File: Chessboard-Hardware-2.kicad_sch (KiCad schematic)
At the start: 1 part, among them J1 Raspberry_Pi_0

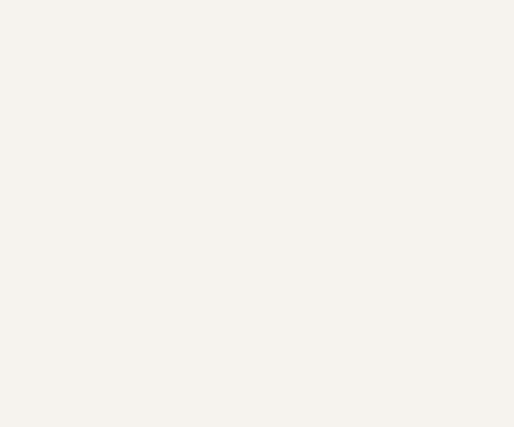
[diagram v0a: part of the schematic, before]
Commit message: Setup for chessboard layout
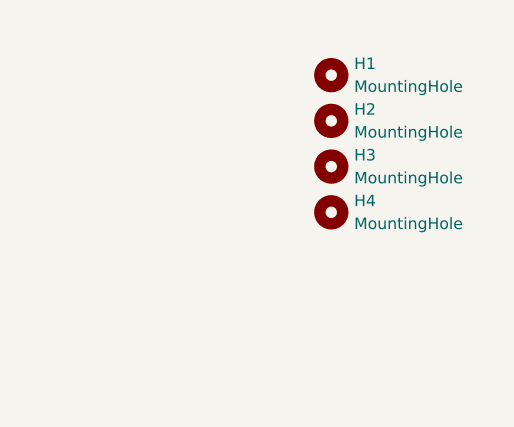
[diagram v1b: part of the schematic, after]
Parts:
- added H1, H2, H3, H4: MountingHole, MountingHole:MountingHole_2.7mm_M2.5, symbol Mechanical:MountingHole

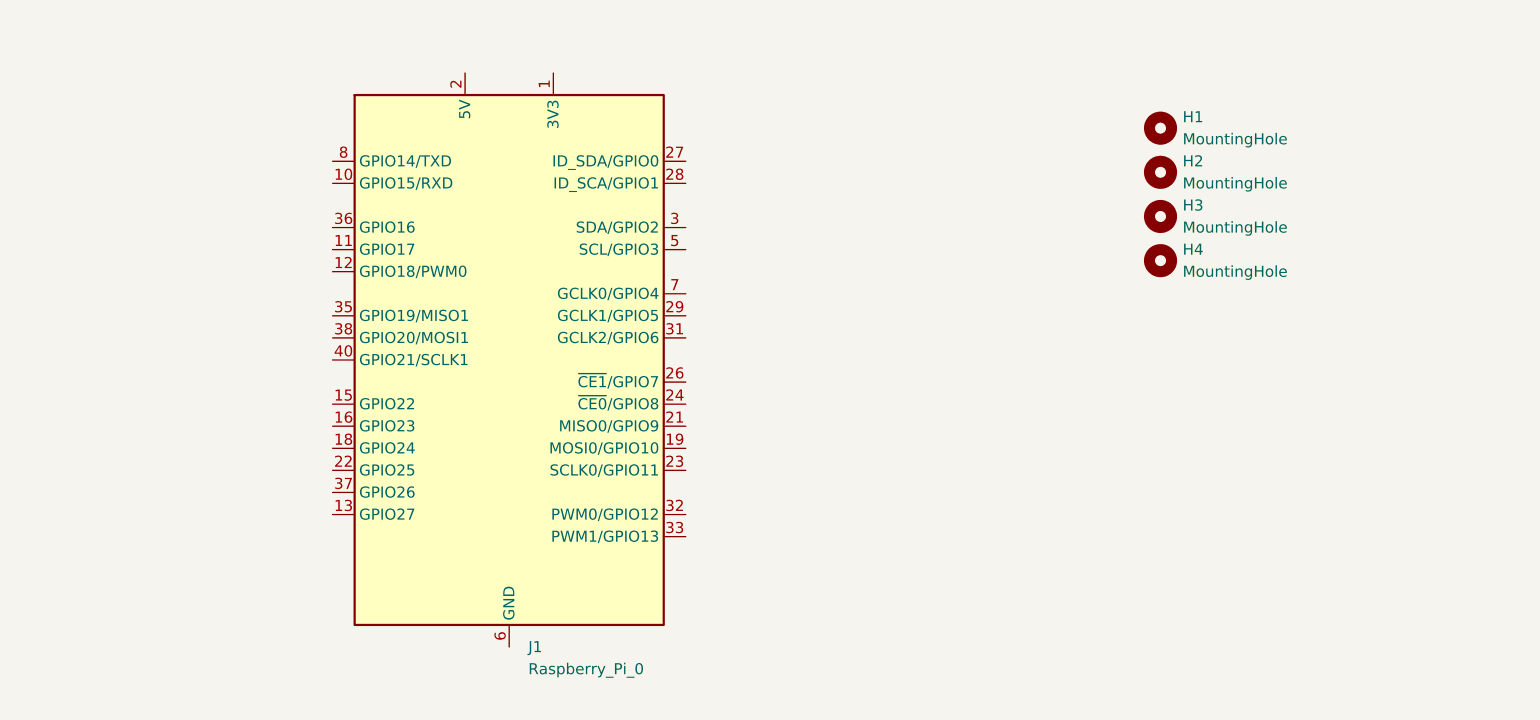
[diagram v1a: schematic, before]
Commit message: Add JST-XH connector and schematic
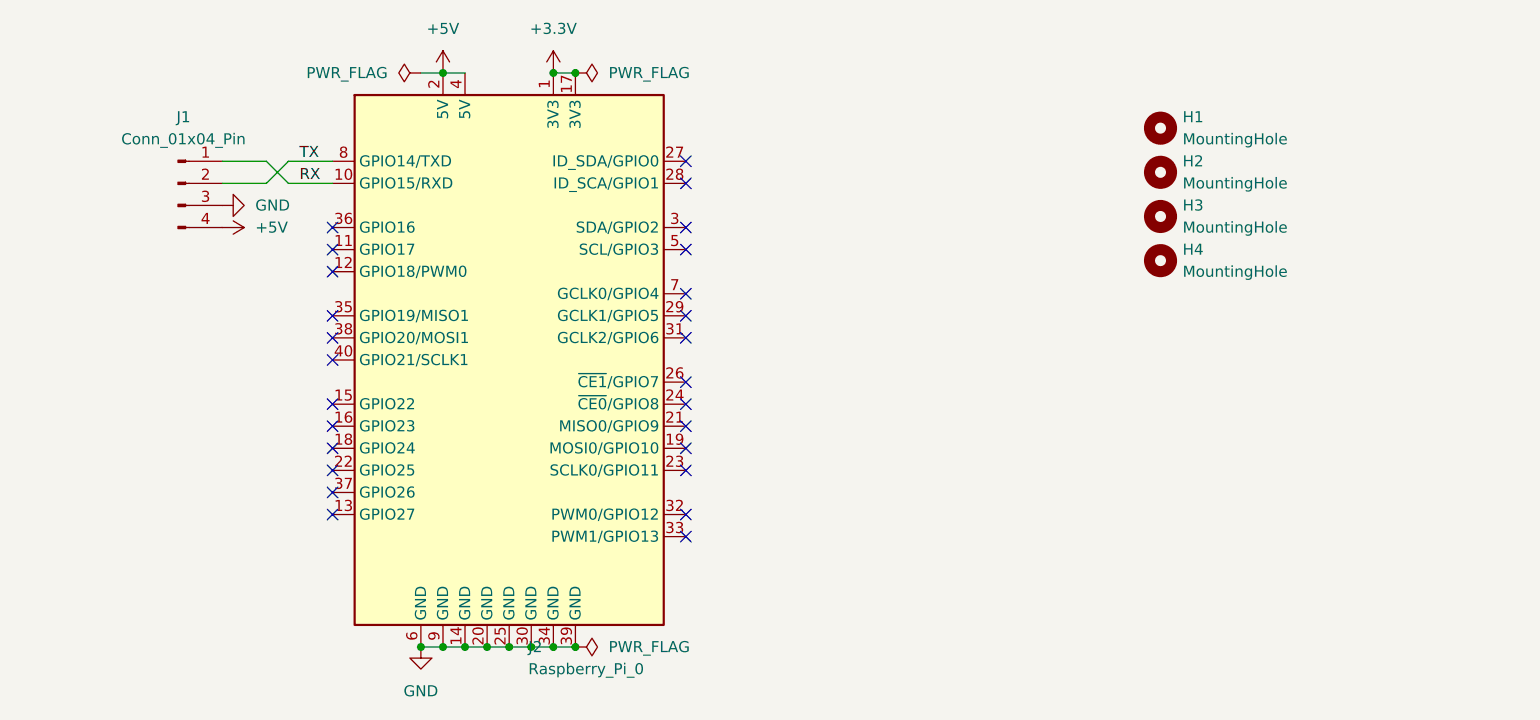
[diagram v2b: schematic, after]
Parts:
- added J1: Conn_01x04_Pin, Connector_JST:JST_XH_B4B-XH-A_1x04_P2.50mm_Vertical, symbol Connector:Conn_01x04_Pin
- renumbered J1 to J2
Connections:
- net 3V3 is gone; now on net +3.3V: J2.17 (3V3)
- net 5V is gone; now on net +5V: J2.4 (5V)
- net GND: now also J2.6 (GND), J1.3 (Pin_3)
- net +3.3V: now reaches J2.1 (3V3)
- net RX: now reaches J2.10 (GPIO15/RXD)
- net RX: now also J1.1 (Pin_1)
- net +5V: now reaches J2.2 (5V)
- net +5V: now also J1.4 (Pin_4)
- net TX: now reaches J2.8 (GPIO14/TXD)
- net TX: now also J1.2 (Pin_2)
- no-connect marks 0 -> 26

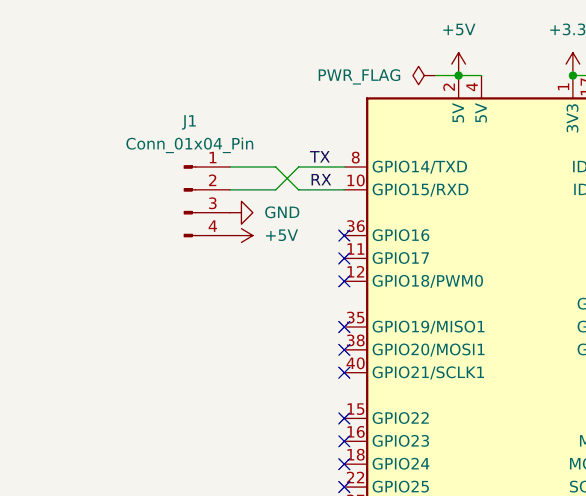
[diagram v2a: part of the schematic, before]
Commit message: Schematic and PCB for wiring up Pi to Nano
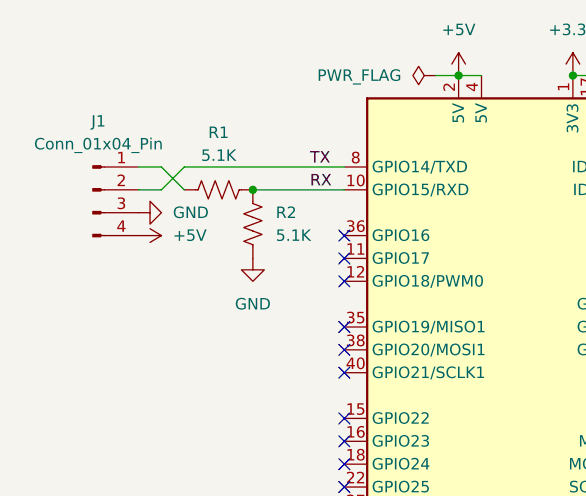
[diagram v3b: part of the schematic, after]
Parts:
- added R1, R2: 5.1K, Resistor_THT:R_Axial_DIN0309_L9.0mm_D3.2mm_P12.70mm_Horizontal, symbol Device:R_US
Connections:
- net GND: now also R2.1
- net RX: now also R1.2, R2.2; no longer J1.1 (Pin_1)
- new net: J1.1 (Pin_1), R1.1
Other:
- moved on the sheet: J1

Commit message: Add test points
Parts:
- added TP1, TP2, TP3, TP4, TP5: TestPoint, Connector_PinHeader_2.54mm:PinHeader_1x01_P2.54mm_Vertical, symbol Connector:TestPoint
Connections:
- net +3.3V: now also TP2.1
- net +5V: now also TP1.1
- net GND: now also TP3.1
- net TX: now also TP4.1
- net at J1.1 (Pin_1), R1.1: now also TP5.1
